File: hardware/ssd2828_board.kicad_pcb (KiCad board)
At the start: 4 copper layers, 91.3 x 35.4 mm, 127 parts, among them IC1 TLV62568DBVR, IC2 MIC5501-3.0YM5-TR, IC3 TPS65131TRGERQ1, J1 FH35C-25S-0.3SHW_50_, J2 FH35C-25S-0.3SHW_50_, J3 Conn_01x34, J4 245863050104829+, J5 503548-1220, J8 FH35C-25S-0.3SHW_50_, U1 SSD2828QN4, U2 PAM2306DYPAA, U3 MIC3289, U4 LP3320, Y1 24mhz

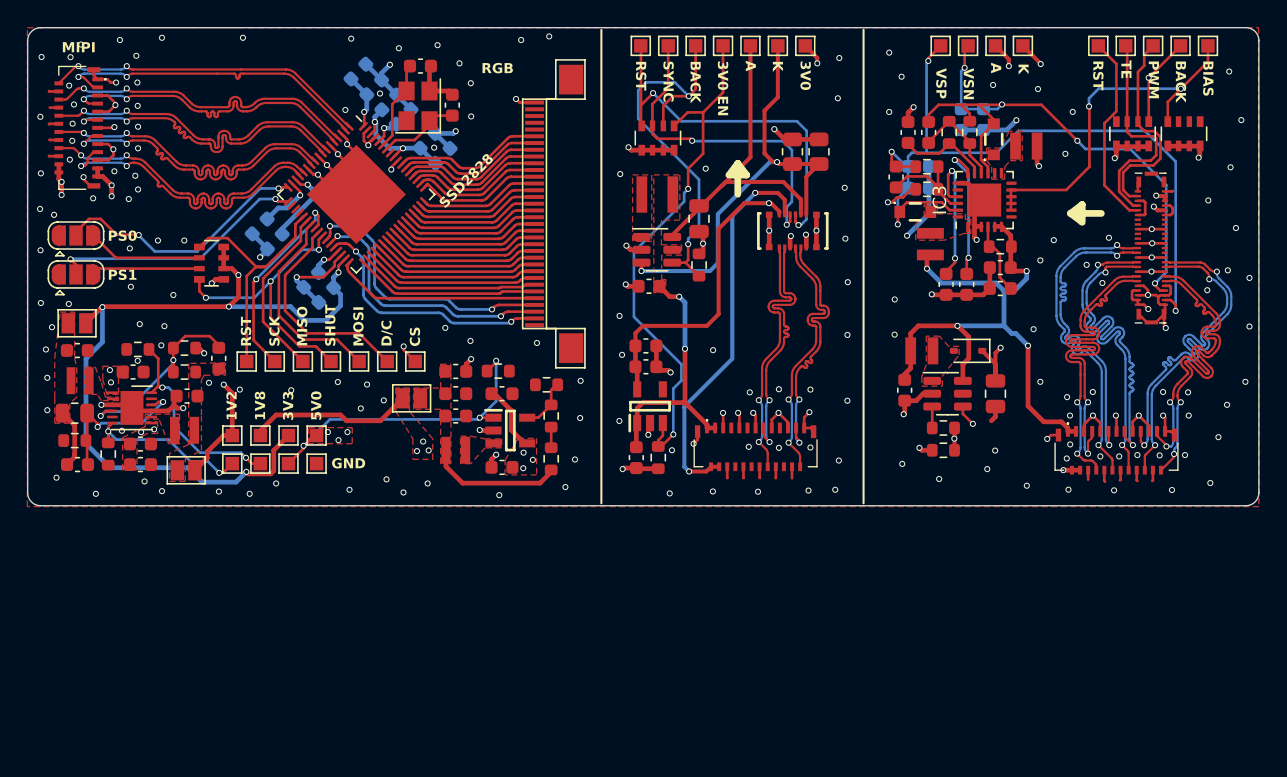
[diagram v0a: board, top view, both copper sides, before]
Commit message: retouched copper fills + started reordering the power nets
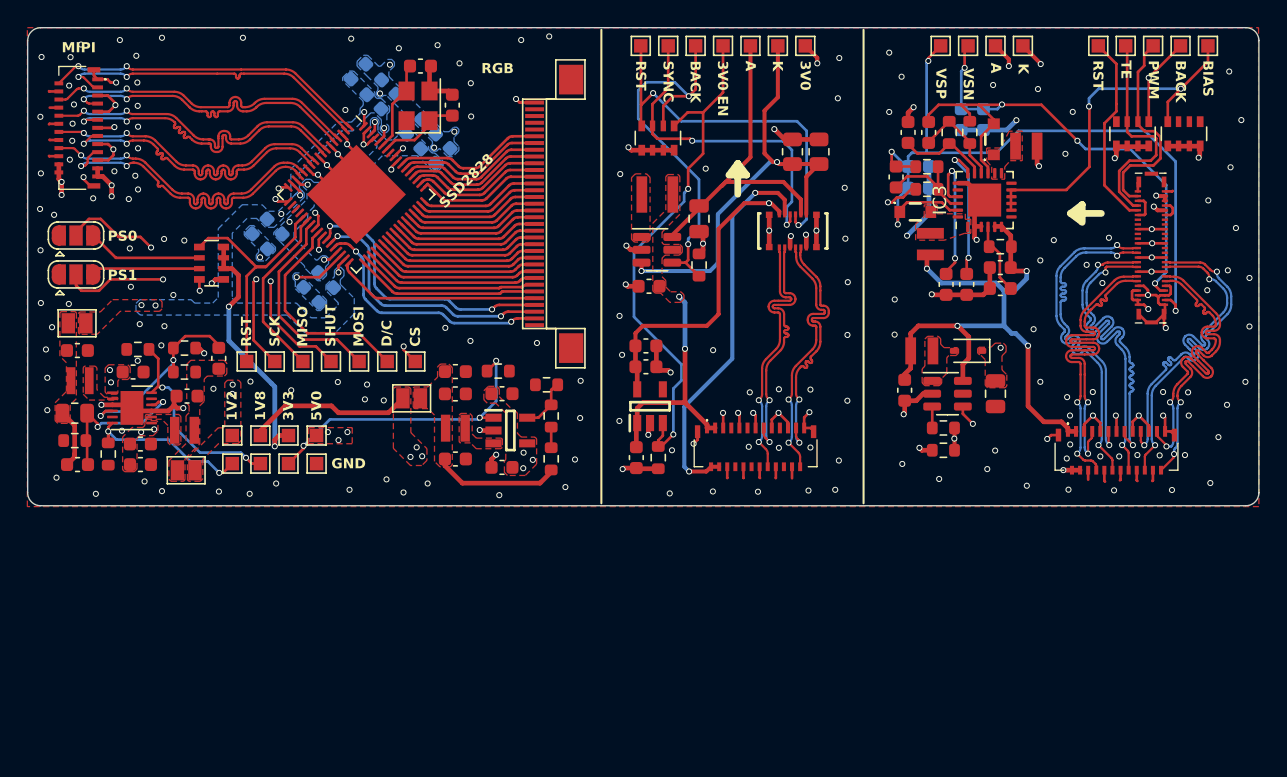
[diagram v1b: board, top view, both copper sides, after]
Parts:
- moved C21 6.49 mm to (83.4, 83.1)
- moved C4 4.09 mm to (81.4, 59.5)
- moved C22 1.64 mm to (83.4, 76.6)
- moved C20 1.64 mm to (83.4, 78.3)
- moved L3 1.64 mm to (83.4, 80.8)
- moved C9 1.59 mm to (78.5, 56.6)
- moved C8 1.45 mm to (80.3, 58.5)
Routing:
- net +3V3: track 88.6 -> 23.5 mm, vias 8 -> 9
- net +1V2: track 56.2 -> 4.68 mm, vias 5 -> 7
- net GND: track 186.4 -> 169.8 mm, vias 217 -> 216
- net +5V: track 72.1 -> 65.7 mm
- net /VS035ZSM/LED_A: track 54.9 -> 49.6 mm
- net Net-(JP3-A): track 10.1 -> 9.40 mm
- added copper zone on B.Cu, net +1V2
- added copper zone on F.Cu, net +1V2
- added copper zone on B.Cu, net +3V3
- added copper zone on F.Cu, net +3V3
- added copper zone on F.Cu, net /VS035ZSM/LED_A
- added copper zone on B.Cu, net GND

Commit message: fixing drc errors + adding debug board for mipi
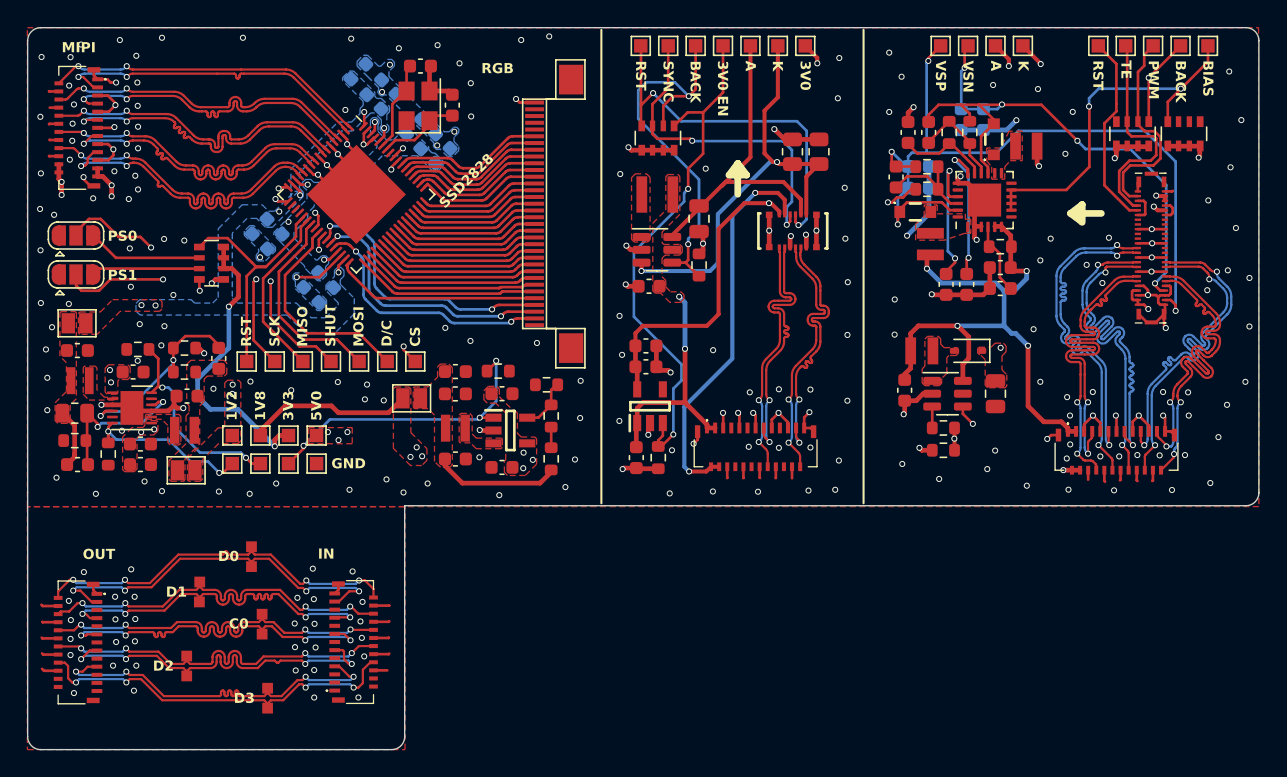
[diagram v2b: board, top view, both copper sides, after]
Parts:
- added J6: FH35C-25S-0.3SHW_50_, SamacSys_Parts:FH35C25S03SHW50, F.Cu at (55.5, 96.7)
- added J7: FH35C-25S-0.3SHW_50_, SamacSys_Parts:FH35C25S03SHW50, F.Cu at (75.8, 96.6)
- added TP32: ~, TestPoint:TestPoint_Pad_0.8x0.8mm, F.Cu at (68.3, 89.6)
- added TP33: ~, TestPoint:TestPoint_Pad_0.8x0.8mm, F.Cu at (68.3, 91.1)
- added TP34: ~, TestPoint:TestPoint_Pad_0.8x0.8mm, F.Cu at (64.5, 92.2)
- added TP35: ~, TestPoint:TestPoint_Pad_0.8x0.8mm, F.Cu at (64.4, 93.7)
- added TP36: ~, TestPoint:TestPoint_Pad_0.8x0.8mm, F.Cu at (69.1, 94.6)
- added TP37: ~, TestPoint:TestPoint_Pad_0.8x0.8mm, F.Cu at (69.1, 96.1)
- added TP38: ~, TestPoint:TestPoint_Pad_0.8x0.8mm, F.Cu at (63.5, 97.7)
- added TP39: ~, TestPoint:TestPoint_Pad_0.8x0.8mm, F.Cu at (63.5, 99.2)
- added TP40: ~, TestPoint:TestPoint_Pad_0.8x0.8mm, F.Cu at (69.5, 101.5)
- added TP41: ~, TestPoint:TestPoint_Pad_0.8x0.8mm, F.Cu at (69.5, 100.1)
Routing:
- net /debug/MIPI_DATA0_N: track 0.00 -> 28.0 mm, vias 0 -> 4
- net /debug/MIPI_DATA0_P: track 0.00 -> 28.0 mm, vias 0 -> 4
- net /debug/MIPI_DATA1_P: track 0.00 -> 27.9 mm, vias 0 -> 4
- net /debug/MIPI_DATA3_P: track 0.00 -> 27.8 mm, vias 0 -> 4
- net /debug/MIPI_CLK_P: track 0.00 -> 27.8 mm, vias 0 -> 4
- net /debug/MIPI_DATA1_N: track 0.00 -> 27.8 mm, vias 0 -> 4
- net /debug/MIPI_CLK_N: track 0.00 -> 27.8 mm, vias 0 -> 4
- net /debug/MIPI_DATA2_P: track 0.00 -> 27.8 mm, vias 0 -> 4
- net /debug/MIPI_DATA2_N: track 0.00 -> 27.8 mm, vias 0 -> 4
- net /debug/MIPI_DATA3_N: track 0.00 -> 27.8 mm, vias 0 -> 4
- net GND: track 169.8 -> 182.9 mm, vias 216 -> 249
- net +3V3: track 23.5 -> 26.6 mm
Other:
- board size 91.3 x 35.4 mm -> 91.3 x 53.5 mm
- board text added: "C0"
- board text added: "D0"
- board text added: "D1"
- board text added: "D2"
- board text added: "D3"
- board text added: "IN"
- board text added: "OUT"

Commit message: routed 1v2 to ssd2828 + finished debug board
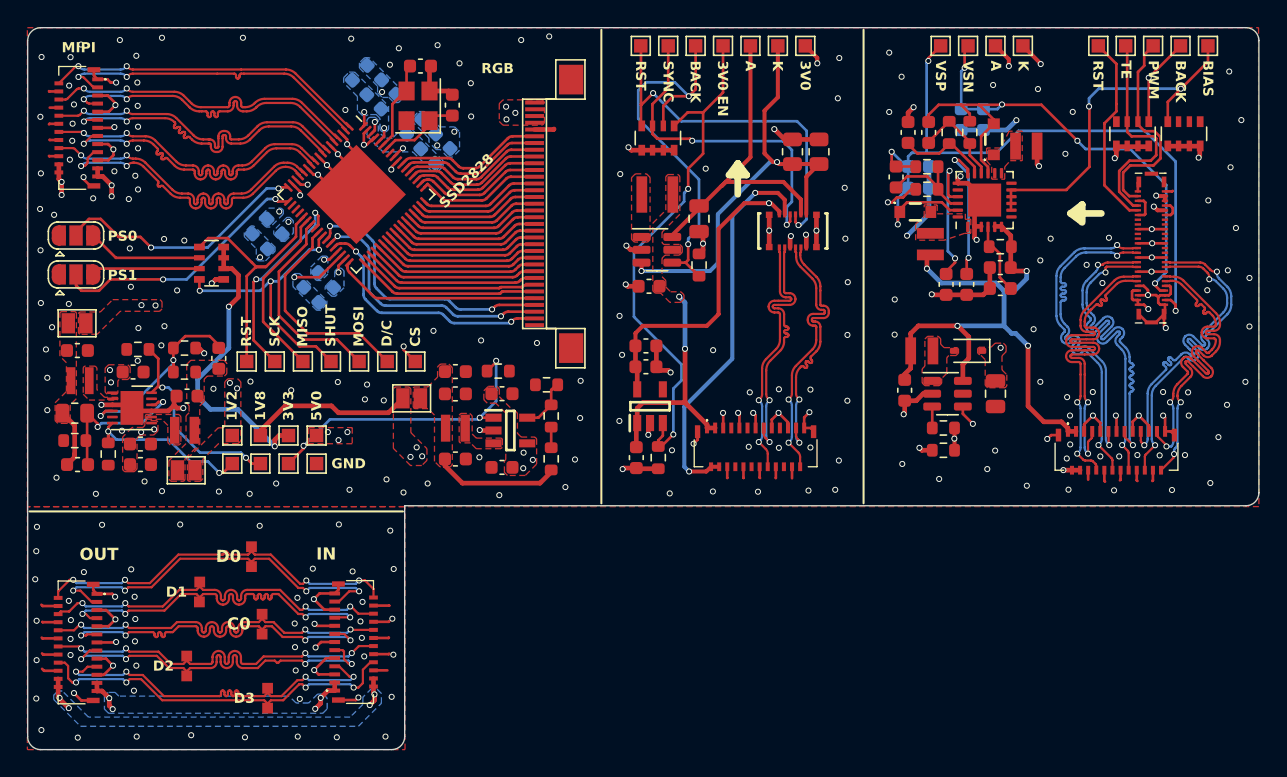
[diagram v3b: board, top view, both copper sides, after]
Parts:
- moved C7 0.14 mm to (76.3, 54.5)
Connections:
- J3 pad 30: unconnected-(J3-Pin_30-Pad30) -> GND
- J3 pad 31: unconnected-(J3-Pin_31-Pad31) -> +5V
- J3 pad 32: unconnected-(J3-Pin_32-Pad32) -> +5V
- J3 pad 33: unconnected-(J3-Pin_33-Pad33) -> +5V
- J3 pad 34: GND -> +5V
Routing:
- net GND: track 182.9 -> 205.5 mm, vias 249 -> 271
- net +5V: track 65.7 -> 71.2 mm, vias 18 -> 25
- net +1V8: track 83.0 -> 87.7 mm, vias 9 -> 13
- added copper zone on In1.Cu, net +1V2
- added copper zone on B.Cu, net +1V8
- added copper zone on In2.Cu, net +3V3
- added copper zone on B.Cu, net +5V

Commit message: finished with vias + fixed board outlines
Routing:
- net GND: track 205.5 -> 201.2 mm, vias 271 -> 278
- net /debug/MIPI_DATA2_N: track 27.8 -> 24.3 mm
- net /debug/MIPI_CLK_P: track 27.8 -> 24.6 mm
- net /debug/MIPI_CLK_N: track 27.8 -> 24.6 mm
- net /VS035ZSM/MIPI_DATA3_P: track 25.3 -> 28.2 mm
- net /debug/MIPI_DATA1_P: track 27.9 -> 25.6 mm
- net /debug/MIPI_DATA1_N: track 27.8 -> 25.6 mm
- net /LH154Q01/MIPI_DATA0_P: track 19.8 -> 18.0 mm
- net /LH154Q01/MIPI_DATA0_N: track 19.8 -> 18.0 mm
- net /LH154Q01/MIPI_CLK_P: track 19.8 -> 18.0 mm
- net /LH154Q01/MIPI_CLK_N: track 19.7 -> 17.9 mm
- net /debug/MIPI_DATA3_P: track 27.8 -> 29.0 mm
- net /debug/MIPI_DATA3_N: track 27.8 -> 28.6 mm
- net +3V0: track 36.9 -> 36.2 mm
- net /debug/MIPI_DATA0_P: track 28.0 -> 28.6 mm
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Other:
- outline, holes or cut-outs redrawn
